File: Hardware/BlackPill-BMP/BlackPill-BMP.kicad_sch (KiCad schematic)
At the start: 41 parts, among them J1 JTAG, J10 Conn_01x12_Male, J2 VCC, J3 GND, J4 SWO, J5 GDB_COMM, J6 TVCC, J7 LogicAna, J8 Conn_01x06_Male, J9 Conn_01x05_Male, U1 BlueAndBlackPill, U2 AD8531ARTZ, U3 74LVC2T45DC, U4 74LS126, U5 74LS126, U6 SRV05-4, U7 SRV05-4

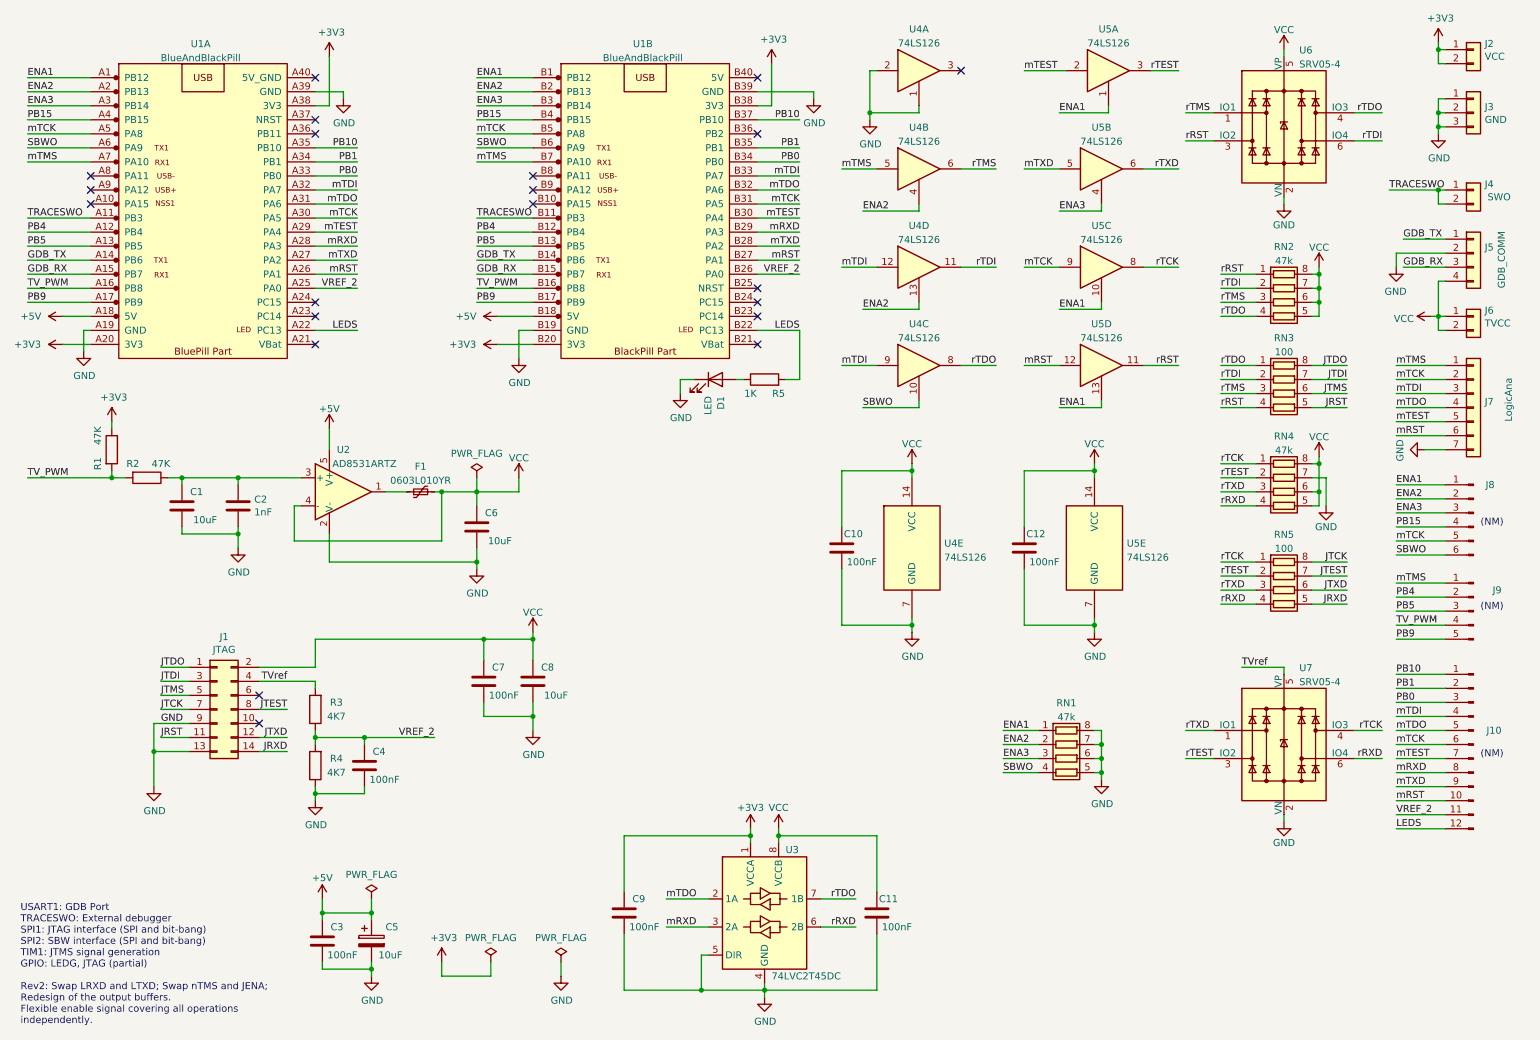
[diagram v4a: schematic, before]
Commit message: Changed output buffer part#
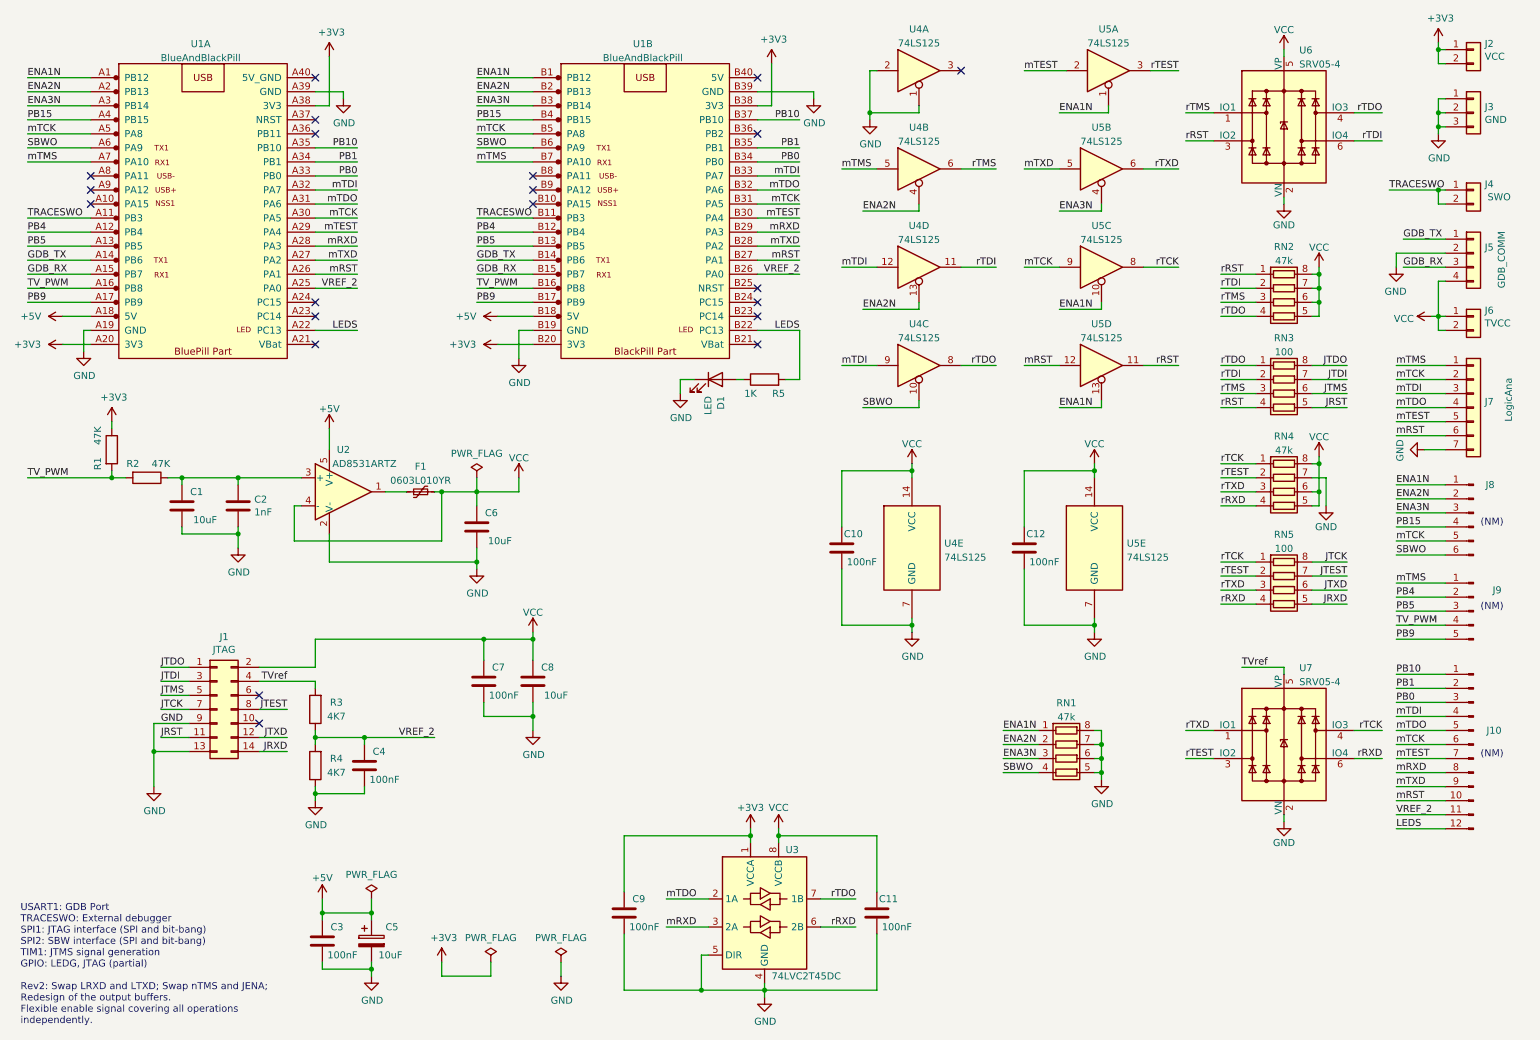
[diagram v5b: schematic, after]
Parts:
- U4, U5: value 74LS126 -> 74LS125; symbol 74xx:74LS126 -> 74xx:74LS125
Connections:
- net ENA1 renamed ENA1N
- net ENA2 renamed ENA2N
- net ENA3 renamed ENA3N
